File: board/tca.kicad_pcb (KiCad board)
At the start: 2 copper layers, 63.5 x 50.8 mm, 27 parts, among them IC1 ATMEGA328-A, P1 CONN_2, P2 CONN_3X2, P3 CONN_8X2, P4 CONN_8X2, P5 CONN_8X2, P6 CONN_8X2, P7 CONN_8X2, P8 CONN_8X2, U1 TLC5941, U2 TLC5941, U3 TLC5941, Y1 RESONATOR

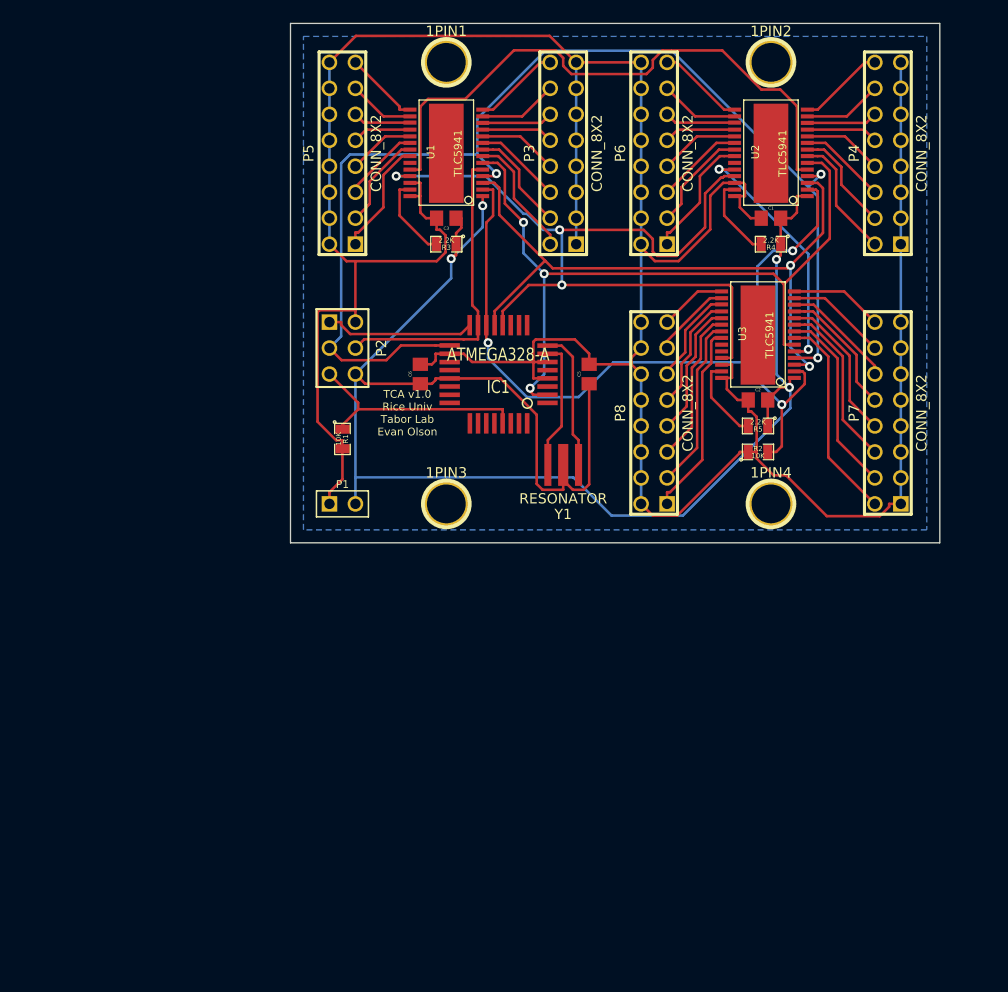
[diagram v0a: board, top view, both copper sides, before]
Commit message: Modified board to include SD card and other improvements.
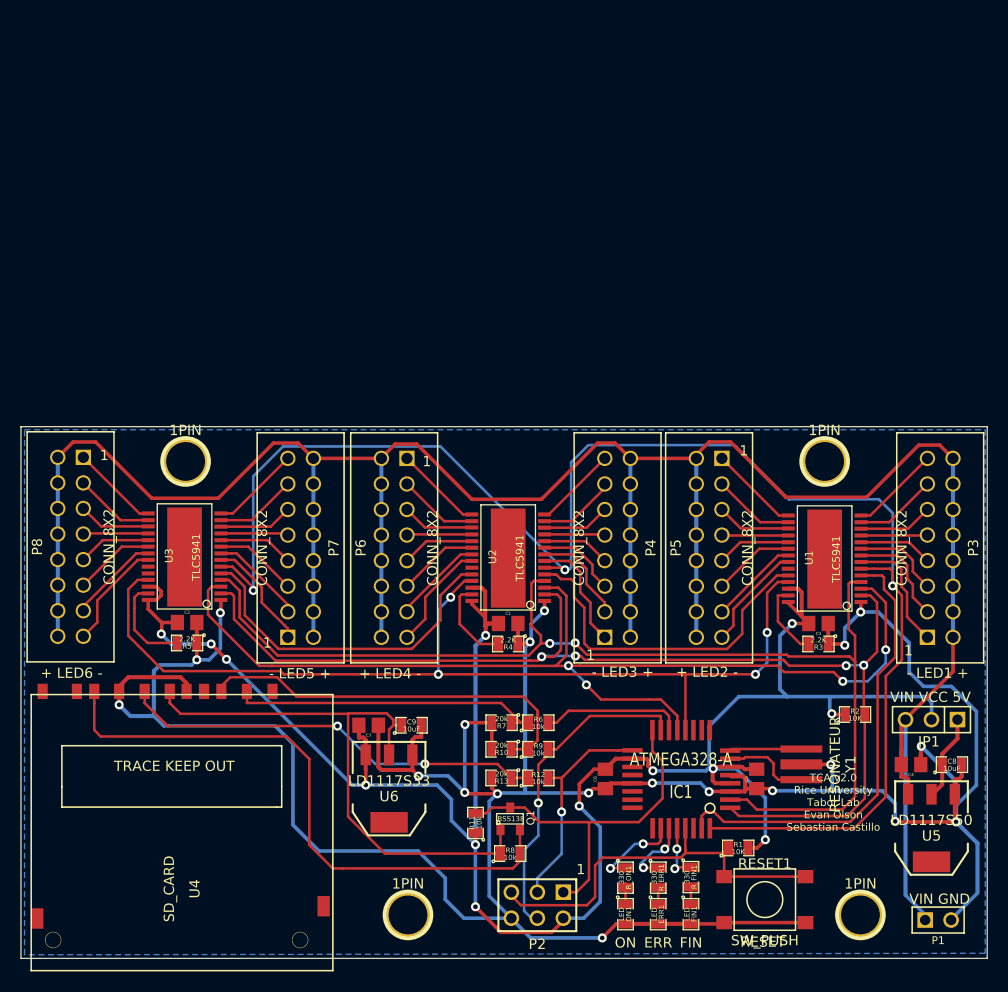
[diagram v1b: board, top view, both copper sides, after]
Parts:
- removed 1PIN1: H1, 1pin
- removed 1PIN2: H2, 1pin
- removed 1PIN3: H3, 1pin
- removed 1PIN4: H4, 1pin
- added 1PIN: P***, hole_ansi_6, F.Cu at (165.0, 129.2)
- added 1PIN: P***, hole_ansi_6, F.Cu at (227.5, 129.2)
- added 1PIN: P***, hole_ansi_6, F.Cu at (186.8, 173.6)
- added 1PIN: P***, hole_ansi_6, F.Cu at (231.0, 173.6)
- added C4: 100nF, c_0805_FIXED, F.Cu at (235.9, 158.8)
- added C7: 100nF, c_0805_FIXED, F.Cu at (182.9, 155.0)
- added C8: 10uF, SM0805, F.Cu at (239.9, 158.8)
- added C9: 10uF, SM0805, F.Cu at (187.1, 155.0)
- added ERR1: LED, SM0805, F.Cu at (211.2, 173.5)
- added FIN1: LED, SM0805, F.Cu at (214.4, 173.5)
- added JP1: JUMPER3, PIN_ARRAY_3X1, F.Cu at (237.9, 154.4)
- added ON1: LED, SM0805, F.Cu at (208.0, 173.5)
- added Q1: BSS138, SOT23, F.Cu at (196.8, 164.2)
- added R10: 20k, SM0805, F.Cu at (195.9, 157.3)
- added R11: 10k, SM0805, F.Cu at (193.3, 164.6)
- added R12: 10k, SM0805, F.Cu at (199.5, 160.2)
- added R13: 20k, SM0805, F.Cu at (195.9, 160.2)
- added R6: 10k, SM0805, F.Cu at (199.5, 154.8)
- added R7: 20k, SM0805, F.Cu at (195.9, 154.8)
- added R8: 10k, SM0805, F.Cu at (196.8, 167.6)
- added R9: 10k, SM0805, F.Cu at (199.5, 157.3)
- added RESET1: SW_PUSH, SW_PUSH_SMD, F.Cu at (221.7, 172.1)
- added R_ERR1: 330, SM0805, F.Cu at (211.2, 169.9)
- added R_FIN1: 330, SM0805, F.Cu at (214.4, 169.8)
- added R_ON1: 330, SM0805, F.Cu at (208.0, 169.9)
- added U4: SD_CARD, SD_CONN, F.Cu at (164.9, 176.0)
- added U5: LD1117S50, SOT223, F.Cu at (237.9, 165.1)
- added U6: LD1117S33, SOT223, F.Cu at (184.9, 161.2)
- P3, P4, P5, P6, P7, P8: footprint pin_array_8x2 -> DF1B_8x2
- Y1: value RESONATOR -> RESONATEUR
- moved P1 71.1 mm to (238.6, 174.1)
- moved U3 60.1 mm to (164.9, 138.6)
- moved C2 59.9 mm to (165.2, 144.9)
- moved R5 59.7 mm to (165.2, 146.9)
- moved P7 58.9 mm to (176.2, 137.7), turned to 270 degrees
- moved P8 58.6 mm to (153.8, 137.6)
- moved P2 57.7 mm to (199.4, 172.6), turned to 180 degrees
- moved R1 55.7 mm to (219.1, 167.0), turned to 0 degrees
- moved U1 54.3 mm to (227.5, 138.8)
- moved C3 53.8 mm to (226.9, 145.1)
- moved R3 53.4 mm to (226.9, 147.1)
- moved P3 53.4 mm to (238.8, 137.7), turned to 270 degrees
- moved P5 52.7 mm to (216.2, 137.7)
- moved C1 47.2 mm to (196.6, 145.1)
- moved U2 47.2 mm to (196.6, 138.7)
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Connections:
- IC1 pad 1: (no net) -> /BLANK
- IC1 pad 14: /BLANK -> /SS
- IC1 pad 2: /MODE -> /SCLK
- IC1 pad 26: (no net) -> /ON
- IC1 pad 27: (no net) -> /ERR
- IC1 pad 28: (no net) -> /FIN
- IC1 pad 3: (no net) -> GND
- IC1 pad 31: (no net) -> /SIN
- IC1 pad 32: (no net) -> /MODE
- IC1 pad 5: (no net) -> GND
- P1 pad 1: /VCC -> /VIN
- P3 pad 1: /VCC -> N-0000018
- P3 pad 10: N-000009 -> /VIN
- P3 pad 11: /VCC -> N-000007
- P3 pad 12: N-0000010 -> /VIN
- P3 pad 13: /VCC -> N-000008
- P3 pad 14: N-000003 (its old number) -> /VIN
- P3 pad 15: /VCC -> N-000009
- P3 pad 16: N-0000011 -> /VIN
- P3 pad 2: N-000005 -> /VIN
- P3 pad 3: /VCC -> N-0000019
- P3 pad 4: N-000006 -> /VIN
- P3 pad 5: /VCC -> N-0000016
- P3 pad 6: N-000007 -> /VIN
- P3 pad 7: /VCC -> N-000005
- P3 pad 8: N-000008 -> /VIN
- P3 pad 9: /VCC -> N-000006
- P4 pad 1: /VCC -> N-0000049
- P4 pad 10: N-0000016 -> /VIN
- P4 pad 11: /VCC -> N-0000054
- P4 pad 12: N-0000017 -> /VIN
- P4 pad 13: /VCC -> N-0000048
- P4 pad 14: N-0000018 -> /VIN
- P4 pad 15: /VCC -> N-0000056
- P4 pad 16: N-0000019 -> /VIN
- P4 pad 2: N-0000012 -> /VIN
- P4 pad 3: /VCC -> N-0000050
- P4 pad 4: N-0000013 -> /VIN
- P4 pad 5: /VCC -> N-0000051
- P4 pad 6: N-0000014 -> /VIN
- P4 pad 7: /VCC -> N-0000052
- P4 pad 8: N-0000015 -> /VIN
- P4 pad 9: /VCC -> N-0000053
- P5 pad 1: N-0000039 -> N-0000017
- P5 pad 10: /VCC -> /VIN
- P5 pad 11: N-0000034 -> N-0000012
- P5 pad 12: /VCC -> /VIN
- P5 pad 13: N-0000033 -> N-0000011
- P5 pad 14: /VCC -> /VIN
- P5 pad 15: N-0000023 -> N-0000010
- P5 pad 16: /VCC -> /VIN
- P5 pad 2: /VCC -> /VIN
- P5 pad 3: N-0000038 -> N-000004
- P5 pad 4: /VCC -> /VIN
- P5 pad 5: N-0000037 -> N-0000015
- P5 pad 6: /VCC -> /VIN
- P5 pad 7: N-0000036 -> N-0000014
- P5 pad 8: /VCC -> /VIN
- P5 pad 9: N-0000035 -> N-0000013
- P6 pad 1: N-0000024 -> N-0000064
- P6 pad 10: /VCC -> /VIN
- P6 pad 11: N-0000029 (its old number) -> N-0000059
- P6 pad 12: /VCC -> /VIN
- P6 pad 13: N-0000030 -> N-0000058
- P6 pad 14: /VCC -> /VIN
- P6 pad 15: N-0000031 -> N-0000057
- P6 pad 16: /VCC -> /VIN
- P6 pad 2: /VCC -> /VIN
- P6 pad 3: N-0000025 -> N-0000063
- P6 pad 4: /VCC -> /VIN
- P6 pad 5: N-0000026 -> N-0000062
- P6 pad 6: /VCC -> /VIN
- P6 pad 7: N-0000027 (its old number) -> N-0000061
- P6 pad 8: /VCC -> /VIN
- P6 pad 9: N-0000028 (its old number) -> N-0000060
- P7 pad 1: /VCC -> N-0000046
- P7 pad 10: N-0000045 -> /VIN
- P7 pad 11: /VCC -> N-0000041
- P7 pad 12: N-0000046 -> /VIN
- P7 pad 13: /VCC -> N-0000040
- P7 pad 14: N-0000047 -> /VIN
- P7 pad 15: /VCC -> N-0000039
- P7 pad 16: N-0000048 -> /VIN
- P7 pad 2: N-0000041 -> /VIN
- P7 pad 3: /VCC -> N-0000045
- P7 pad 4: N-0000042 -> /VIN
- P7 pad 5: /VCC -> N-0000044
- P7 pad 6: N-0000043 -> /VIN
- P7 pad 7: /VCC -> N-0000043
- P7 pad 8: N-0000044 -> /VIN
- P7 pad 9: /VCC -> N-0000042
- P8 pad 1: N-0000040 -> N-0000076
- P8 pad 10: /VCC -> /VIN
- P8 pad 11: N-0000053 -> N-0000071
- P8 pad 12: /VCC -> /VIN
- P8 pad 13: N-0000054 -> N-0000055
- P8 pad 14: /VCC -> /VIN
- P8 pad 15: N-0000055 -> N-0000047
- P8 pad 16: /VCC -> /VIN
- P8 pad 2: /VCC -> /VIN
- P8 pad 3: N-0000049 -> N-0000075
- P8 pad 4: /VCC -> /VIN
- P8 pad 5: N-0000050 -> N-0000074
- P8 pad 6: /VCC -> /VIN
- P8 pad 7: N-0000051 -> N-0000073
- P8 pad 8: /VCC -> /VIN
- P8 pad 9: N-0000052 -> N-0000072
- U1 pad 10: N-000008 -> N-000005
- U1 pad 11: N-000009 -> N-000006
- U1 pad 12: N-0000010 -> N-000007
- U1 pad 13: N-000003 (its old number) -> N-000008
- U1 pad 14: N-0000011 -> N-000009
- U1 pad 15: N-0000023 -> N-0000017
- U1 pad 16: N-0000033 -> N-000004
- U1 pad 17: N-0000034 -> N-0000015
- U1 pad 18: N-0000035 -> N-0000014
- U1 pad 19: N-0000036 -> N-0000013
- U1 pad 20: N-0000037 -> N-0000012
- U1 pad 21: N-0000038 -> N-0000011
- U1 pad 22: N-0000039 -> N-0000010
- U1 pad 4: /SCK -> /SCLK
- U1 pad 5: /MOSI -> /SIN
- U1 pad 7: N-000005 -> N-0000018
- U1 pad 8: N-000006 -> N-0000019
- U1 pad 9: N-000007 -> N-0000016
- U2 pad 10: N-0000015 -> N-0000052
- U2 pad 11: N-0000016 -> N-0000053
- U2 pad 12: N-0000017 -> N-0000054
- U2 pad 13: N-0000018 -> N-0000048
- U2 pad 14: N-0000019 -> N-0000056
- U2 pad 15: N-0000031 -> N-0000064
- U2 pad 16: N-0000030 -> N-0000063
- U2 pad 17: N-0000029 (its old number) -> N-0000062
- U2 pad 18: N-0000028 (its old number) -> N-0000061
- U2 pad 19: N-0000027 (its old number) -> N-0000060
- U2 pad 20: N-0000026 -> N-0000059
- U2 pad 21: N-0000025 -> N-0000058
- U2 pad 22: N-0000024 -> N-0000057
- U2 pad 4: /SCK -> /SCLK
- U2 pad 7: N-0000012 -> N-0000049
- U2 pad 8: N-0000013 -> N-0000050
- U2 pad 9: N-0000014 -> N-0000051
- U3 pad 10: N-0000044 -> N-0000043
- U3 pad 11: N-0000045 -> N-0000042
- U3 pad 12: N-0000046 -> N-0000041
- U3 pad 13: N-0000047 -> N-0000040
- U3 pad 14: N-0000048 -> N-0000039
- U3 pad 15: N-0000055 -> N-0000076
- U3 pad 16: N-0000054 -> N-0000075
- U3 pad 17: N-0000053 -> N-0000074
- U3 pad 18: N-0000052 -> N-0000073
- U3 pad 19: N-0000051 -> N-0000072
- U3 pad 20: N-0000050 -> N-0000071
- U3 pad 21: N-0000049 -> N-0000055
- U3 pad 22: N-0000040 -> N-0000047
- U3 pad 4: /SCK -> /SCLK
- U3 pad 7: N-0000041 -> N-0000046
- U3 pad 8: N-0000042 -> N-0000045
- U3 pad 9: N-0000043 -> N-0000044
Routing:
- net /VIN: track 0.00 -> 249.6 mm
- net GND: track 164.2 -> 308.8 mm, vias 4 -> 20
- net /SCLK: track 0.00 -> 111.1 mm, vias 0 -> 2
- net /VCC: track 305.3 -> 203.5 mm, vias 0 -> 13
- net /SCK: track 115.9 -> 21.5 mm, vias 3 -> 1
- net /MODE: track 74.4 -> 152.0 mm
- net /SD_DataOut: track 0.00 -> 59.3 mm
- net /VSD: track 0.00 -> 56.9 mm
- net /SIN: track 0.00 -> 44.8 mm
- net /SD_SCLK: track 0.00 -> 41.7 mm, vias 0 -> 2
- net /XLAT: track 66.4 -> 106.3 mm, vias 2 -> 4
- net /SD_DataIn: track 0.00 -> 39.0 mm
- net /SD_CS: track 0.00 -> 30.4 mm
- net /BLANK: track 84.6 -> 112.9 mm, vias 3 -> 4
- net N-0000027: track 58.6 -> 34.1 mm
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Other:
- board size 63.5 x 50.8 mm -> 94.5 x 52 mm
- net class Power added: clearance 0.254, trace_width 0.35, via_dia 0.889, via_drill 0.635
- board text added: "+ LED2 -"
- board text added: "+ LED4 -"
- board text added: "+ LED6 -"
- board text added: "- LED1 +"
- board text added: "- LED3 +"
- board text added: "- LED5 +"
- board text added: "1"
- board text added: "ERR"
- board text added: "FIN"
- board text added: "ON"
- board text added: "RESET"
- board text added: "TCA v2.0 Rice University Tabor Lab Evan Olson Sebastian Castillo"
- board text added: "VIN GND"
- board text added: "VIN VCC 5V"
- board text removed: "TCA v1.0 Rice Univ Tabor Lab Evan Olson"
